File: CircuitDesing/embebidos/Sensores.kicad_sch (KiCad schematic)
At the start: 5 parts

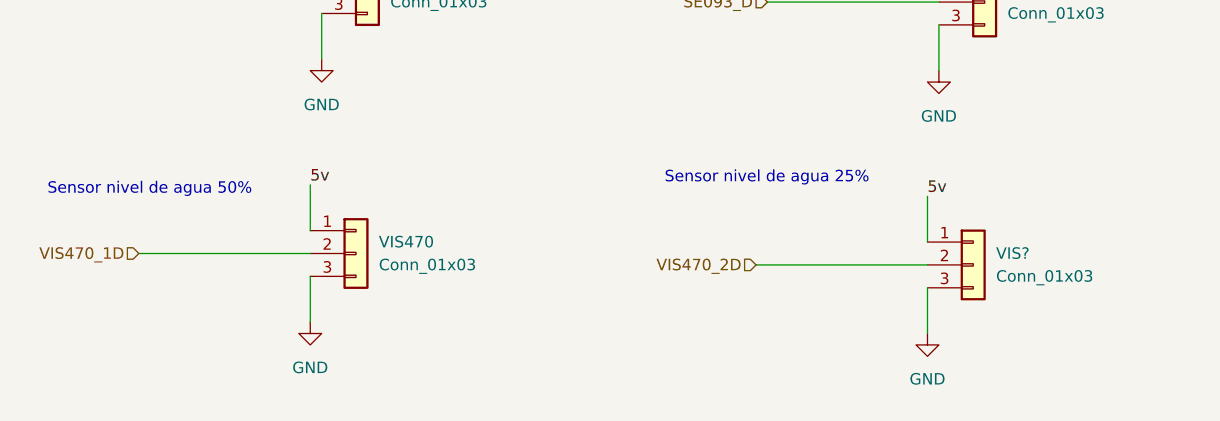
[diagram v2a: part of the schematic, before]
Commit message: Sensor Ultrasonido
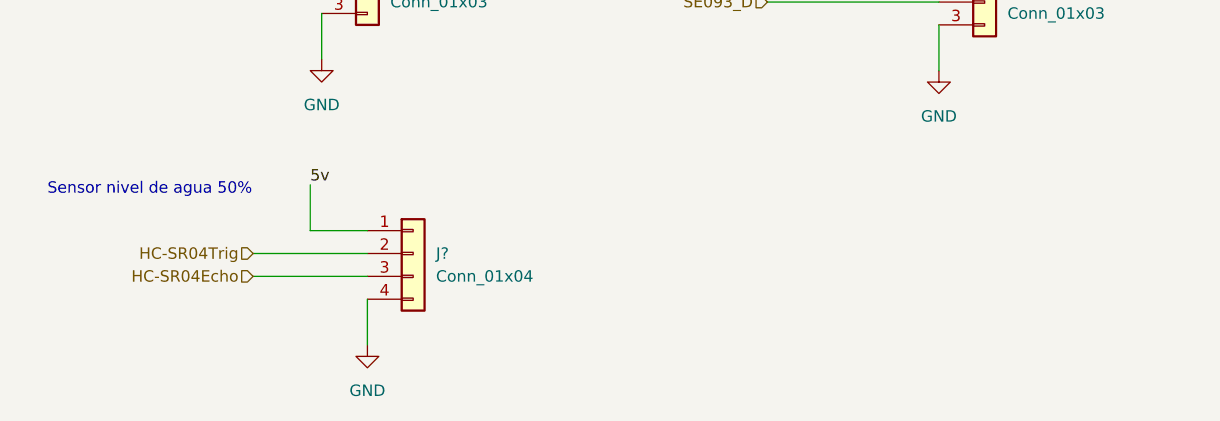
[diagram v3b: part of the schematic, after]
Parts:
- removed VIS470, VIS?: Conn_01x03, symbol Connector_Generic:Conn_01x03
- added J?: Conn_01x04, symbol Connector_Generic:Conn_01x04
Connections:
- net 5v: now also J?.1 (Pin_1)
- net GND: now also J?.4 (Pin_4)
- new net HC-SR04Echo: J?.3 (Pin_3)
- new net HC-SR04Trig: J?.2 (Pin_2)
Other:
- note removed: "Sensor nivel de agua 25%"
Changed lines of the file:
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@@
-    (stroke (width 0) (type default) (color 0 0 0 0))
-  )
-  (wire (pts (xy 137.16 130.81) (xy 137.16 135.89))
     (stroke (width 0) (type default) (color 0 0 0 0))
   )
@@
     (stroke (width 0) (type default) (color 0 0 0 0))
   )
+  (wire (pts (xy 62.23 129.54) (xy 74.93 129.54))
+    (stroke (width 0) (type default) (color 0 0 0 0))
+  )
   (wire (pts (xy 69.85 90.17) (xy 69.85 95.25))
     (stroke (width 0) (type default) (color 0 0 0 0))
   )
-  (wire (pts (xy 118.11 128.27) (xy 137.16 128.27))
+  (wire (pts (xy 62.23 127) (xy 74.93 127))
+    (stroke (width 0) (type default) (color 0 0 0 0))
+  )
+  (wire (pts (xy 68.58 124.46) (xy 74.93 124.46))
     (stroke (width 0) (type default) (color 0 0 0 0))
   )
@@
     (stroke (width 0) (type default) (color 0 0 0 0))
   )
-  (wire (pts (xy 68.58 129.54) (xy 68.58 134.62))
+  (wire (pts (xy 74.93 132.08) (xy 74.93 137.16))
     (stroke (width 0) (type default) (color 0 0 0 0))
   )
@@
     (stroke (width 0) (type default) (color 0 0 0 0))
   )
-  (wire (pts (xy 49.53 127) (xy 68.58 127))
-    (stroke (width 0) (type default) (color 0 0 0 0))
-  )
-  (wire (pts (xy 137.16 120.65) (xy 137.16 125.73))
-    (stroke (width 0) (type default) (color 0 0 0 0))
-  )
   (wire (pts (xy 111.76 64.77) (xy 120.65 64.77))
     (stroke (width 0) (type default) (color 0 0 0 0))
@@
     (effects (font (size 1.27 1.27)) (justify left bottom))
   )
-  (text "Sensor nivel de agua 25%" (at 107.95 119.38 0)
-    (effects (font (size 1.27 1.27)) (justify left bottom))
-  )
   (text "Sensor de iluminación" (at 120.65 57.15 0)
     (effects (font (size 1.27 1.27)) (justify left bottom))
@@
     (effects (font (size 1.27 1.27)) (justify left bottom))
   )
-  (label "5v" (at 137.16 120.65 0)
-    (effects (font (size 1.27 1.27)) (justify left bottom))
-  )
   (label "5v" (at 138.43 91.44 0)
     (effects (font (size 1.27 1.27)) (justify left bottom))
@@
     (effects (font (size 1.27 1.27)) (justify right))
   )
+  (hierarchical_label "HC-SR04Trig" (shape input) (at 62.23 127 180)
+    (effects (font (size 1.27 1.27)) (justify right))
+  )
   (hierarchical_label "5v" (shape input) (at 45.72 40.64 180)
     (effects (font (size 1.27 1.27)) (justify right))
   )
-  (hierarchical_label "VIS470_2D" (shape input) (at 118.11 128.27 180)
-    (effects (font (size 1.27 1.27)) (justify right))
-  )
-  (hierarchical_label "VIS470_1D" (shape input) (at 49.53 127 180)
+  (hierarchical_label "HC-SR04Echo" (shape input) (at 62.23 129.54 180)
     (effects (font (size 1.27 1.27)) (justify right))
   )
@@
     (effects (font (size 1.27 1.27)) (justify right))
   )
+  (symbol (lib_id "Connector_Generic:Conn_01x04") (at 80.01 127 0) (unit 1)
+    (in_bom yes) (on_board yes) (fields_autoplaced)
+    (property "Reference" "J?" (id 0) (at 82.55 126.9999 0)
+      (effects (font (size 1.27 1.27)) (justify left))
+    )
+    (property "Value" "Conn_01x04" (id 1) (at 82.55 129.5399 0)
+      (effects (font (size 1.27 1.27)) (justify left))
+    )
+    (property "Footprint" "" (id 2) (at 80.01 127 0)
+      (effects (font (size 1.27 1.27)) hide)
+    )
+    (property "Datasheet" "~" (id 3) (at 80.01 127 0)
+      (effects (font (size 1.27 1.27)) hide)
+    )
+    (pin "1")
+    (pin "2")
+    (pin "3")
+    (pin "4")
+  )
   (symbol (lib_id "Connector_Generic:Conn_01x03") (at 143.51 99.06 0) (unit 1)
     (in_bom yes) (on_board yes) (fields_autoplaced)
@@
     (pin "2")
     (pin "3")
-  )
-  (symbol (lib_id "power:GND") (at 137.16 135.89 0) (unit 1)
-    (in_bom yes) (on_board yes) (fields_autoplaced)
-    (property "Reference" "#PWR?" (id 0) (at 137.16 142.24 0)
-      (effects (font (size 1.27 1.27)) hide)
-    )
-    (property "Value" "GND" (id 1) (at 137.16 140.97 0))
-    (property "Footprint" "" (id 2) (at 137.16 135.89 0)
-      (effects (font (size 1.27 1.27)) hide)
-    )
-    (property "Datasheet" "" (id 3) (at 137.16 135.89 0)
-      (effects (font (size 1.27 1.27)) hide)
-    )
-    (pin "1")
   )
   (symbol (lib_id "Connector_Generic:Conn_01x03") (at 74.93 64.77 0) (unit 1)
@@
     (pin "3")
   )
-  (symbol (lib_id "Connector_Generic:Conn_01x03") (at 142.24 128.27 0) (unit 1)
-    (in_bom yes) (on_board yes) (fields_autoplaced)
-    (property "Reference" "VIS?" (id 0) (at 144.78 126.9999 0)
-      (effects (font (size 1.27 1.27)) (justify left))
-    )
-    (property "Value" "Conn_01x03" (id 1) (at 144.78 129.5399 0)
-      (effects (font (size 1.27 1.27)) (justify left))
-    )
-    (property "Footprint" "" (id 2) (at 142.24 128.27 0)
-      (effects (font (size 1.27 1.27)) hide)
-    )
-    (property "Datasheet" "~" (id 3) (at 142.24 128.27 0)
-      (effects (font (size 1.27 1.27)) hide)
-    )
-    (pin "1")
-    (pin "2")
-    (pin "3")
-  )
-  (symbol (lib_id "power:GND") (at 68.58 134.62 0) (unit 1)
-    (in_bom yes) (on_board yes) (fields_autoplaced)
-    (property "Reference" "#PWR?" (id 0) (at 68.58 140.97 0)
-      (effects (font (size 1.27 1.27)) hide)
-    )
-    (property "Value" "GND" (id 1) (at 68.58 139.7 0))
-    (property "Footprint" "" (id 2) (at 68.58 134.62 0)
-      (effects (font (size 1.27 1.27)) hide)
-    )
-    (property "Datasheet" "" (id 3) (at 68.58 134.62 0)
-      (effects (font (size 1.27 1.27)) hide)
-    )
-    (pin "1")
-  )
-  (symbol (lib_id "Connector_Generic:Conn_01x03") (at 73.66 127 0) (unit 1)
-    (in_bom yes) (on_board yes) (fields_autoplaced)
-    (property "Reference" "VIS470" (id 0) (at 76.2 125.7299 0)
-      (effects (font (size 1.27 1.27)) (justify left))
-    )
-    (property "Value" "Conn_01x03" (id 1) (at 76.2 128.2699 0)
-      (effects (font (size 1.27 1.27)) (justify left))
-    )
-    (property "Footprint" "" (id 2) (at 73.66 127 0)
-      (effects (font (size 1.27 1.27)) hide)
-    )
-    (property "Datasheet" "~" (id 3) (at 73.66 127 0)
-      (effects (font (size 1.27 1.27)) hide)
-    )
-    (pin "1")
-    (pin "2")
-    (pin "3")
+  (symbol (lib_id "power:GND") (at 74.93 137.16 0) (unit 1)
+    (in_bom yes) (on_board yes) (fields_autoplaced)
+    (property "Reference" "#PWR?" (id 0) (at 74.93 143.51 0)
+      (effects (font (size 1.27 1.27)) hide)
+    )
+    (property "Value" "GND" (id 1) (at 74.93 142.24 0))
+    (property "Footprint" "" (id 2) (at 74.93 137.16 0)
+      (effects (font (size 1.27 1.27)) hide)
+    )
+    (property "Datasheet" "" (id 3) (at 74.93 137.16 0)
+      (effects (font (size 1.27 1.27)) hide)
+    )
+    (pin "1")
   )
   (symbol (lib_id "power:GND") (at 69.85 72.39 0) (unit 1)

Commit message: Huellas parciales
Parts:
- gave numbers to parts that had none: 1
- renumbered SE093 to SE93
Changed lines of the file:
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@@
   (symbol (lib_id "Connector_Generic:Conn_01x04") (at 80.01 127 0) (unit 1)
     (in_bom yes) (on_board yes) (fields_autoplaced)
-    (property "Reference" "J?" (id 0) (at 82.55 126.9999 0)
+    (property "Reference" "HC-SR4" (id 0) (at 82.55 126.9999 0)
       (effects (font (size 1.27 1.27)) (justify left))
     )
@@
   (symbol (lib_id "Connector_Generic:Conn_01x03") (at 143.51 99.06 0) (unit 1)
     (in_bom yes) (on_board yes) (fields_autoplaced)
-    (property "Reference" "SE093" (id 0) (at 146.05 97.7899 0)
+    (property "Reference" "SE93" (id 0) (at 146.05 97.7899 0)
       (effects (font (size 1.27 1.27)) (justify left))
     )
@@
   (symbol (lib_id "power:GND") (at 69.85 105.41 0) (unit 1)
     (in_bom yes) (on_board yes) (fields_autoplaced)
-    (property "Reference" "#PWR?" (id 0) (at 69.85 111.76 0)
+    (property "Reference" "#PWR04" (id 0) (at 69.85 111.76 0)
       (effects (font (size 1.27 1.27)) hide)
     )
@@
   (symbol (lib_id "power:GND") (at 138.43 106.68 0) (unit 1)
     (in_bom yes) (on_board yes) (fields_autoplaced)
-    (property "Reference" "#PWR?" (id 0) (at 138.43 113.03 0)
+    (property "Reference" "#PWR06" (id 0) (at 138.43 113.03 0)
       (effects (font (size 1.27 1.27)) hide)
     )
@@
   (symbol (lib_id "power:GND") (at 74.93 137.16 0) (unit 1)
     (in_bom yes) (on_board yes) (fields_autoplaced)
-    (property "Reference" "#PWR?" (id 0) (at 74.93 143.51 0)
+    (property "Reference" "#PWR05" (id 0) (at 74.93 143.51 0)
       (effects (font (size 1.27 1.27)) hide)
     )
@@
   (symbol (lib_id "power:GND") (at 69.85 72.39 0) (unit 1)
     (in_bom yes) (on_board yes) (fields_autoplaced)
-    (property "Reference" "#PWR?" (id 0) (at 69.85 78.74 0)
+    (property "Reference" "#PWR03" (id 0) (at 69.85 78.74 0)
       (effects (font (size 1.27 1.27)) hide)
     )

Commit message: 15 footprints faltantes
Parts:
- HC-SR4: footprint (none) -> Connector_JST:JST_EH_B4B-EH-A_1x04_P2.50mm_Vertical
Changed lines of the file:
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@@
       (effects (font (size 1.27 1.27)) (justify left))
     )
-    (property "Footprint" "" (id 2) (at 80.01 127 0)
+    (property "Footprint" "Connector_JST:JST_EH_B4B-EH-A_1x04_P2.50mm_Vertical" (id 2) (at 80.01 127 0)
       (effects (font (size 1.27 1.27)) hide)
     )

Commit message: Todas las huellas
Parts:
- DHT11_1, DHT11_2, SE93: footprint (none) -> Connector_JST:JST_EH_B3B-EH-A_1x03_P2.50mm_Vertical
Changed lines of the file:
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@@
       (effects (font (size 1.27 1.27)) (justify left))
     )
-    (property "Footprint" "" (id 2) (at 143.51 99.06 0)
+    (property "Footprint" "Connector_JST:JST_EH_B3B-EH-A_1x03_P2.50mm_Vertical" (id 2) (at 143.51 99.06 0)
       (effects (font (size 1.27 1.27)) hide)
     )
@@
       (effects (font (size 1.27 1.27)) (justify left))
     )
-    (property "Footprint" "" (id 2) (at 74.93 64.77 0)
+    (property "Footprint" "Connector_JST:JST_EH_B3B-EH-A_1x03_P2.50mm_Vertical" (id 2) (at 74.93 64.77 0)
       (effects (font (size 1.27 1.27)) hide)
     )
@@
       (effects (font (size 1.27 1.27)) (justify left))
     )
-    (property "Footprint" "" (id 2) (at 74.93 97.79 0)
+    (property "Footprint" "Connector_JST:JST_EH_B3B-EH-A_1x03_P2.50mm_Vertical" (id 2) (at 74.93 97.79 0)
       (effects (font (size 1.27 1.27)) hide)
     )

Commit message: pull up
Circuito LDR
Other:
- sheet Sensor de iluminacion ports: added 3.3v; removed none
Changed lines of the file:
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@@
+    (stroke (width 0) (type default) (color 0 0 0 0))
+  )
+  (wire (pts (xy 45.72 45.72) (xy 50.8 45.72))
     (stroke (width 0) (type default) (color 0 0 0 0))
   )
@@
     (stroke (width 0) (type default) (color 0 0 0 0))
   )
+  (wire (pts (xy 113.03 72.39) (xy 120.65 72.39))
+    (stroke (width 0) (type default) (color 0 0 0 0))
+  )
   (text "Sensor de humedad de aire y temperatura" (at 40.64 91.44 0)
     (effects (font (size 1.27 1.27)) (justify left bottom))
@@
     (effects (font (size 1.27 1.27)) (justify left bottom))
   )
+  (label "3.3v" (at 113.03 72.39 180)
+    (effects (font (size 1.27 1.27)) (justify right bottom))
+  )
   (label "5v" (at 111.76 59.69 0)
     (effects (font (size 1.27 1.27)) (justify left bottom))
@@
     (effects (font (size 1.27 1.27)) (justify left bottom))
   )
+  (label "3.3v" (at 50.8 45.72 0)
+    (effects (font (size 1.27 1.27)) (justify left bottom))
+  )
   (label "5v" (at 69.85 57.15 0)
     (effects (font (size 1.27 1.27)) (justify left bottom))
@@
   )
   (hierarchical_label "HC-SR04Trig" (shape input) (at 62.23 127 180)
+    (effects (font (size 1.27 1.27)) (justify right))
+  )
+  (hierarchical_label "3.3v" (shape input) (at 45.72 45.72 180)
     (effects (font (size 1.27 1.27)) (justify right))
   )
@@
       (effects (font (size 1.27 1.27)) (justify left))
     )
+    (pin "3.3v" input (at 120.65 72.39 180)
+      (effects (font (size 1.27 1.27)) (justify left))
+    )

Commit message: Actualizacion huellas
Huellas+Programador
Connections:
- net 3.3v: now also DHT11_1.1 (Pin_1), DHT11_2.1 (Pin_1), SE93.1 (Pin_1)
- net 5v: no longer DHT11_1.1 (Pin_1), DHT11_2.1 (Pin_1), SE93.1 (Pin_1)
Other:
- moved on the sheet: HC-SR4, SE93
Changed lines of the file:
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@@
     (stroke (width 0) (type default) (color 0 0 0 0))
   )
-  (wire (pts (xy 138.43 91.44) (xy 138.43 96.52))
+  (wire (pts (xy 69.85 118.11) (xy 69.85 123.19))
     (stroke (width 0) (type default) (color 0 0 0 0))
   )
@@
     (stroke (width 0) (type default) (color 0 0 0 0))
   )
-  (wire (pts (xy 138.43 101.6) (xy 138.43 106.68))
-    (stroke (width 0) (type default) (color 0 0 0 0))
-  )
-  (wire (pts (xy 68.58 119.38) (xy 68.58 124.46))
-    (stroke (width 0) (type default) (color 0 0 0 0))
-  )
-  (wire (pts (xy 62.23 129.54) (xy 74.93 129.54))
+  (wire (pts (xy 69.85 128.27) (xy 69.85 133.35))
+    (stroke (width 0) (type default) (color 0 0 0 0))
+  )
+  (wire (pts (xy 135.89 95.25) (xy 135.89 100.33))
+    (stroke (width 0) (type default) (color 0 0 0 0))
+  )
+  (wire (pts (xy 129.54 105.41) (xy 142.24 105.41))
     (stroke (width 0) (type default) (color 0 0 0 0))
   )
@@
     (stroke (width 0) (type default) (color 0 0 0 0))
   )
-  (wire (pts (xy 62.23 127) (xy 74.93 127))
-    (stroke (width 0) (type default) (color 0 0 0 0))
-  )
-  (wire (pts (xy 68.58 124.46) (xy 74.93 124.46))
+  (wire (pts (xy 129.54 102.87) (xy 142.24 102.87))
+    (stroke (width 0) (type default) (color 0 0 0 0))
+  )
+  (wire (pts (xy 135.89 100.33) (xy 142.24 100.33))
     (stroke (width 0) (type default) (color 0 0 0 0))
   )
@@
     (stroke (width 0) (type default) (color 0 0 0 0))
   )
-  (wire (pts (xy 74.93 132.08) (xy 74.93 137.16))
-    (stroke (width 0) (type default) (color 0 0 0 0))
-  )
-  (wire (pts (xy 119.38 99.06) (xy 138.43 99.06))
+  (wire (pts (xy 142.24 107.95) (xy 142.24 113.03))
+    (stroke (width 0) (type default) (color 0 0 0 0))
+  )
+  (wire (pts (xy 50.8 125.73) (xy 69.85 125.73))
     (stroke (width 0) (type default) (color 0 0 0 0))
   )
@@
     (effects (font (size 1.27 1.27)) (justify left bottom))
   )
-  (text "Sensor de humedad de suelo" (at 109.22 92.71 0)
+  (text "Sensor de humedad de suelo" (at 40.64 119.38 0)
     (effects (font (size 1.27 1.27)) (justify left bottom))
   )
@@
     (effects (font (size 1.27 1.27)) (justify left bottom))
   )
-  (text "Sensor nivel de agua 50%" (at 39.37 120.65 0)
+  (text "Sensor nivel de agua 50%" (at 106.68 96.52 0)
     (effects (font (size 1.27 1.27)) (justify left bottom))
   )
@@
     (effects (font (size 1.27 1.27)) (justify left bottom))
   )
-  (label "5v" (at 68.58 119.38 0)
+  (label "5v" (at 135.89 95.25 0)
     (effects (font (size 1.27 1.27)) (justify left bottom))
   )
@@
     (effects (font (size 1.27 1.27)) (justify left bottom))
   )
-  (label "5v" (at 69.85 57.15 0)
-    (effects (font (size 1.27 1.27)) (justify left bottom))
-  )
-  (label "5v" (at 69.85 90.17 0)
-    (effects (font (size 1.27 1.27)) (justify left bottom))
-  )
-  (label "5v" (at 138.43 91.44 0)
+  (label "3.3v" (at 69.85 57.15 0)
+    (effects (font (size 1.27 1.27)) (justify left bottom))
+  )
+  (label "3.3v" (at 69.85 90.17 0)
+    (effects (font (size 1.27 1.27)) (justify left bottom))
+  )
+  (label "3.3v" (at 69.85 118.11 0)
     (effects (font (size 1.27 1.27)) (justify left bottom))
   )
@@
     (effects (font (size 1.27 1.27)) (justify right))
   )
-  (hierarchical_label "SE093_D" (shape input) (at 119.38 99.06 180)
-    (effects (font (size 1.27 1.27)) (justify right))
-  )
-  (hierarchical_label "HC-SR04Trig" (shape input) (at 62.23 127 180)
+  (hierarchical_label "SE093_D" (shape input) (at 50.8 125.73 180)
+    (effects (font (size 1.27 1.27)) (justify right))
+  )
+  (hierarchical_label "HC-SR04Trig" (shape input) (at 129.54 102.87 180)
     (effects (font (size 1.27 1.27)) (justify right))
   )
@@
     (effects (font (size 1.27 1.27)) (justify right))
   )
-  (hierarchical_label "HC-SR04Echo" (shape input) (at 62.23 129.54 180)
+  (hierarchical_label "HC-SR04Echo" (shape input) (at 129.54 105.41 180)
     (effects (font (size 1.27 1.27)) (justify right))
   )
@@
     (effects (font (size 1.27 1.27)) (justify right))
   )
-  (symbol (lib_id "Connector_Generic:Conn_01x04") (at 80.01 127 0) (unit 1)
-    (in_bom yes) (on_board yes) (fields_autoplaced)
-    (property "Reference" "HC-SR4" (id 0) (at 82.55 126.9999 0)
-      (effects (font (size 1.27 1.27)) (justify left))
-    )
-    (property "Value" "Conn_01x04" (id 1) (at 82.55 129.5399 0)
-      (effects (font (size 1.27 1.27)) (justify left))
-    )
-    (property "Footprint" "Connector_JST:JST_EH_B4B-EH-A_1x04_P2.50mm_Vertical" (id 2) (at 80.01 127 0)
-      (effects (font (size 1.27 1.27)) hide)
-    )
-    (property "Datasheet" "~" (id 3) (at 80.01 127 0)
+  (symbol (lib_id "Connector_Generic:Conn_01x04") (at 147.32 102.87 0) (unit 1)
+    (in_bom yes) (on_board yes) (fields_autoplaced)
+    (property "Reference" "HC-SR4" (id 0) (at 149.86 102.8699 0)
+      (effects (font (size 1.27 1.27)) (justify left))
+    )
+    (property "Value" "Conn_01x04" (id 1) (at 149.86 105.4099 0)
+      (effects (font (size 1.27 1.27)) (justify left))
+    )
+    (property "Footprint" "Connector_JST:JST_EH_B4B-EH-A_1x04_P2.50mm_Vertical" (id 2) (at 147.32 102.87 0)
+      (effects (font (size 1.27 1.27)) hide)
+    )
+    (property "Datasheet" "~" (id 3) (at 147.32 102.87 0)
       (effects (font (size 1.27 1.27)) hide)
     )
@@
     (pin "4")
   )
-  (symbol (lib_id "Connector_Generic:Conn_01x03") (at 143.51 99.06 0) (unit 1)
-    (in_bom yes) (on_board yes) (fields_autoplaced)
-    (property "Reference" "SE93" (id 0) (at 146.05 97.7899 0)
-      (effects (font (size 1.27 1.27)) (justify left))
-    )
-    (property "Value" "Conn_01x03" (id 1) (at 146.05 100.3299 0)
-      (effects (font (size 1.27 1.27)) (justify left))
-    )
-    (property "Footprint" "Connector_JST:JST_EH_B3B-EH-A_1x03_P2.50mm_Vertical" (id 2) (at 143.51 99.06 0)
-      (effects (font (size 1.27 1.27)) hide)
-    )
-    (property "Datasheet" "~" (id 3) (at 143.51 99.06 0)
+  (symbol (lib_id "Connector_Generic:Conn_01x03") (at 74.93 125.73 0) (unit 1)
+    (in_bom yes) (on_board yes) (fields_autoplaced)
+    (property "Reference" "SE93" (id 0) (at 77.47 124.4599 0)
+      (effects (font (size 1.27 1.27)) (justify left))
+    )
+    (property "Value" "Conn_01x03" (id 1) (at 77.47 126.9999 0)
+      (effects (font (size 1.27 1.27)) (justify left))
+    )
+    (property "Footprint" "Connector_JST:JST_EH_B3B-EH-A_1x03_P2.50mm_Vertical" (id 2) (at 74.93 125.73 0)
+      (effects (font (size 1.27 1.27)) hide)
+    )
+    (property "Datasheet" "~" (id 3) (at 74.93 125.73 0)
       (effects (font (size 1.27 1.27)) hide)
     )
@@
     (pin "1")
   )
-  (symbol (lib_id "power:GND") (at 138.43 106.68 0) (unit 1)
-    (in_bom yes) (on_board yes) (fields_autoplaced)
-    (property "Reference" "#PWR06" (id 0) (at 138.43 113.03 0)
-      (effects (font (size 1.27 1.27)) hide)
-    )
-    (property "Value" "GND" (id 1) (at 138.43 111.76 0))
-    (property "Footprint" "" (id 2) (at 138.43 106.68 0)
-      (effects (font (size 1.27 1.27)) hide)
-    )
-    (property "Datasheet" "" (id 3) (at 138.43 106.68 0)
+  (symbol (lib_id "power:GND") (at 69.85 133.35 0) (unit 1)
+    (in_bom yes) (on_board yes) (fields_autoplaced)
+    (property "Reference" "#PWR06" (id 0) (at 69.85 139.7 0)
+      (effects (font (size 1.27 1.27)) hide)
+    )
+    (property "Value" "GND" (id 1) (at 69.85 138.43 0))
+    (property "Footprint" "" (id 2) (at 69.85 133.35 0)
+      (effects (font (size 1.27 1.27)) hide)
+    )
+    (property "Datasheet" "" (id 3) (at 69.85 133.35 0)
       (effects (font (size 1.27 1.27)) hide)
     )
@@
     (pin "3")
   )
-  (symbol (lib_id "power:GND") (at 74.93 137.16 0) (unit 1)
-    (in_bom yes) (on_board yes) (fields_autoplaced)
-    (property "Reference" "#PWR05" (id 0) (at 74.93 143.51 0)
-      (effects (font (size 1.27 1.27)) hide)
-    )
-    (property "Value" "GND" (id 1) (at 74.93 142.24 0))
-    (property "Footprint" "" (id 2) (at 74.93 137.16 0)
-      (effects (font (size 1.27 1.27)) hide)
-    )
-    (property "Datasheet" "" (id 3) (at 74.93 137.16 0)
-      (effects (font (size 1.27 1.27)) hide)
-    )
+  (symbol (lib_id "power:GND") (at 142.24 113.03 0) (unit 1)
+    (in_bom yes) (on_board yes) (fields_autoplaced)
+    (property "Reference" "#PWR05" (id 0) (at 142.24 119.38 0)
+      (effects (font (size 1.27 1.27)) hide)
+    )
+    (property "Value" "GND" (id 1) (at 142.24 118.11 0))
+    (property "Footprint" "" (id 2) (at 142.24 113.03 0)
+      (effects (font (size 1.27 1.27)) hide)
+    )
+    (property "Datasheet" "" (id 3) (at 142.24 113.03 0)
+      (effects (font (size 1.27 1.27)) hide)
+    )
